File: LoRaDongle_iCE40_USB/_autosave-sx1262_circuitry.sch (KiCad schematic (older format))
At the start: 38 parts

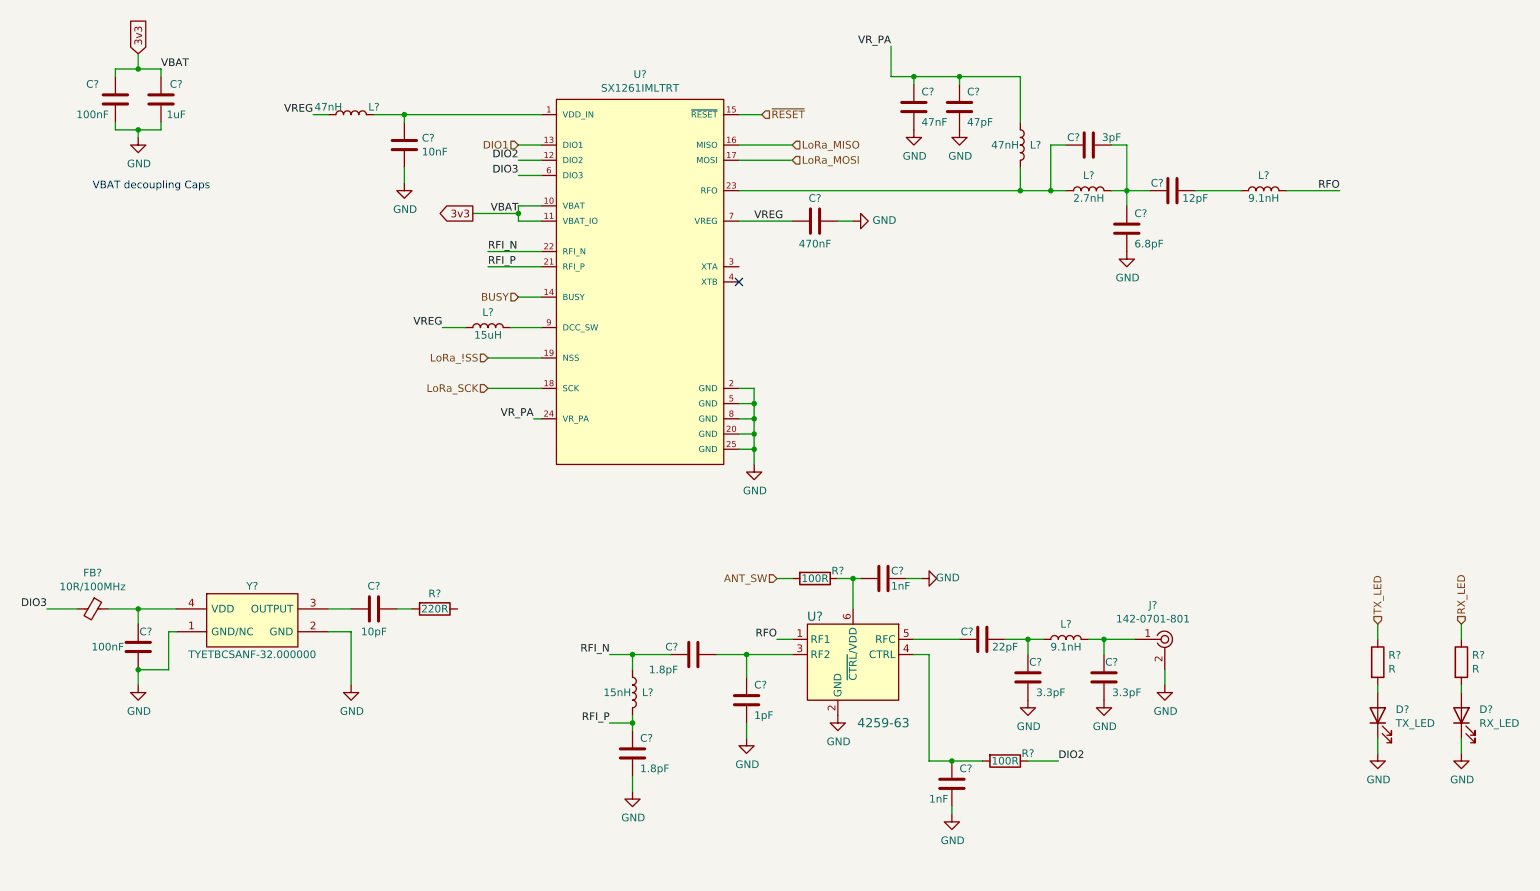
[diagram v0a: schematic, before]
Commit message: changed to sx1261
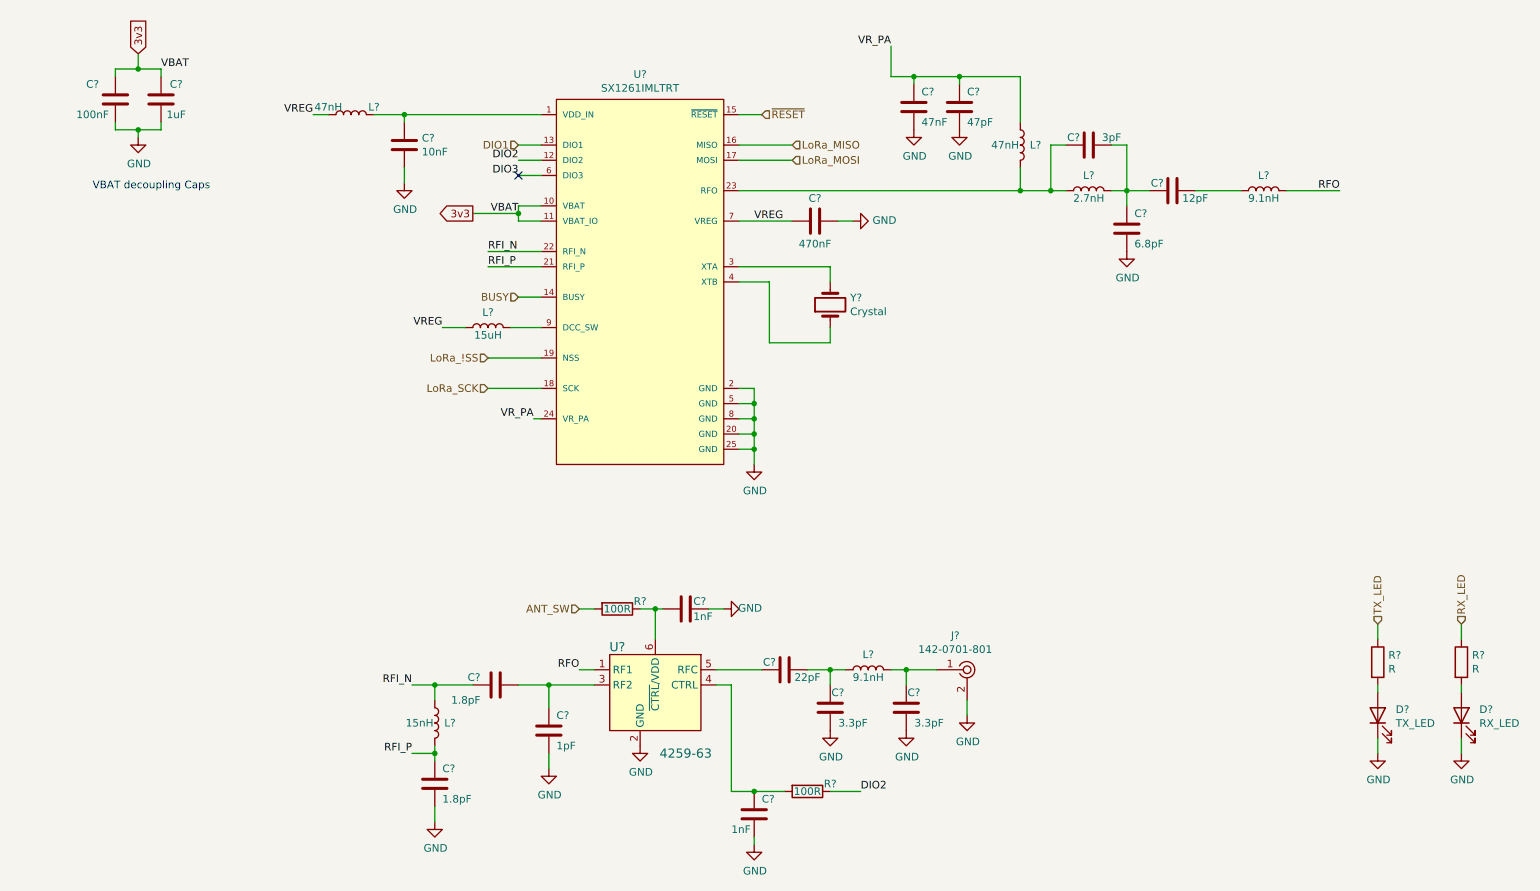
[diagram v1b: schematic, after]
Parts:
- removed C?: 100nF, Capacitor_SMD:C_0402_1005Metric, symbol Device:C
- removed C?: 10pF, Capacitor_SMD:C_0402_1005Metric, symbol Device:C
- removed FB?: 10R/100MHz, Inductor_SMD:L_0402_1005Metric, symbol Device:Ferrite_Bead_Small
- removed R?: 220R, Resistor_SMD:R_0402_1005Metric, symbol Device:R
- removed Y?: TYETBCSANF-32.000000, TY, symbol TYETBCSANF-32.000000:TYETBCSANF-32.000000
- added Y?: Crystal, Crystal:Crystal_SMD_2016-4Pin_2.0x1.6mm, symbol Device:Crystal
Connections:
- net at U?.3 (XTA): now also Y?.2
- net at U?.4 (XTB): now also Y?.1
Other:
- moved on the sheet: C?, J?, L?, R?, U?
